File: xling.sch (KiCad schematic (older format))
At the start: 61 parts, among them J1 ISP, J2 USB_OTG, J3 Battery, Q1 NTR0202PL, SW1 BTN, SW2 BTN, SW3 BTN, U1 REX012864L, U2 ATmega1284P-AU, U3 MCP73831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

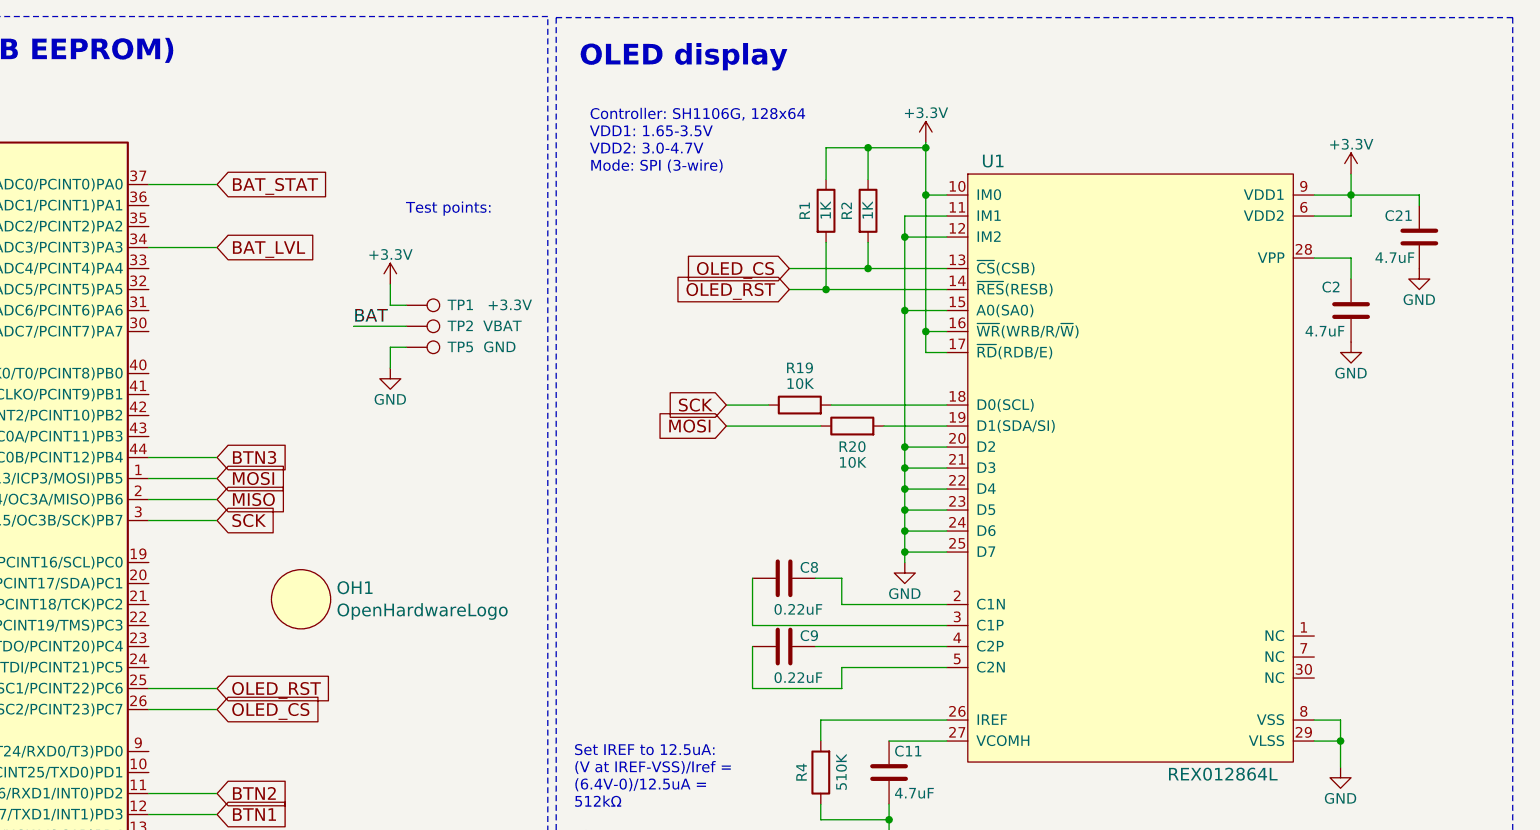
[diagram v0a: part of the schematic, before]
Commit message: patch 3.1: More checkpoints and 4-wire SPI.
This is the first commit after version adjustment and in a new
current/3.0 branch. All of the changes in the third iteration of the
Xling PCB will find their place in this branch.

Starting from Xling PCB v3.1, new checkpoints are available:

    +3.3V - output voltage of the power supply block and AP3401
            particularly;
    VBAT - Li-Ion battery voltage;
    SCK - SCK pin of the SPI;
    MOSI - MOSI pin of the SPI;
    CS - Chip-select pin of the OLED display;
    DC - Data/Command pin of the OLED display;
    RST - Reset pin of the OLED display;
    GND - Ground of the PCB.

And the display is connected via 4-wire SPI from now on.

Signed-off-by: Dmitry Salychev <dsl@mcusim.org>
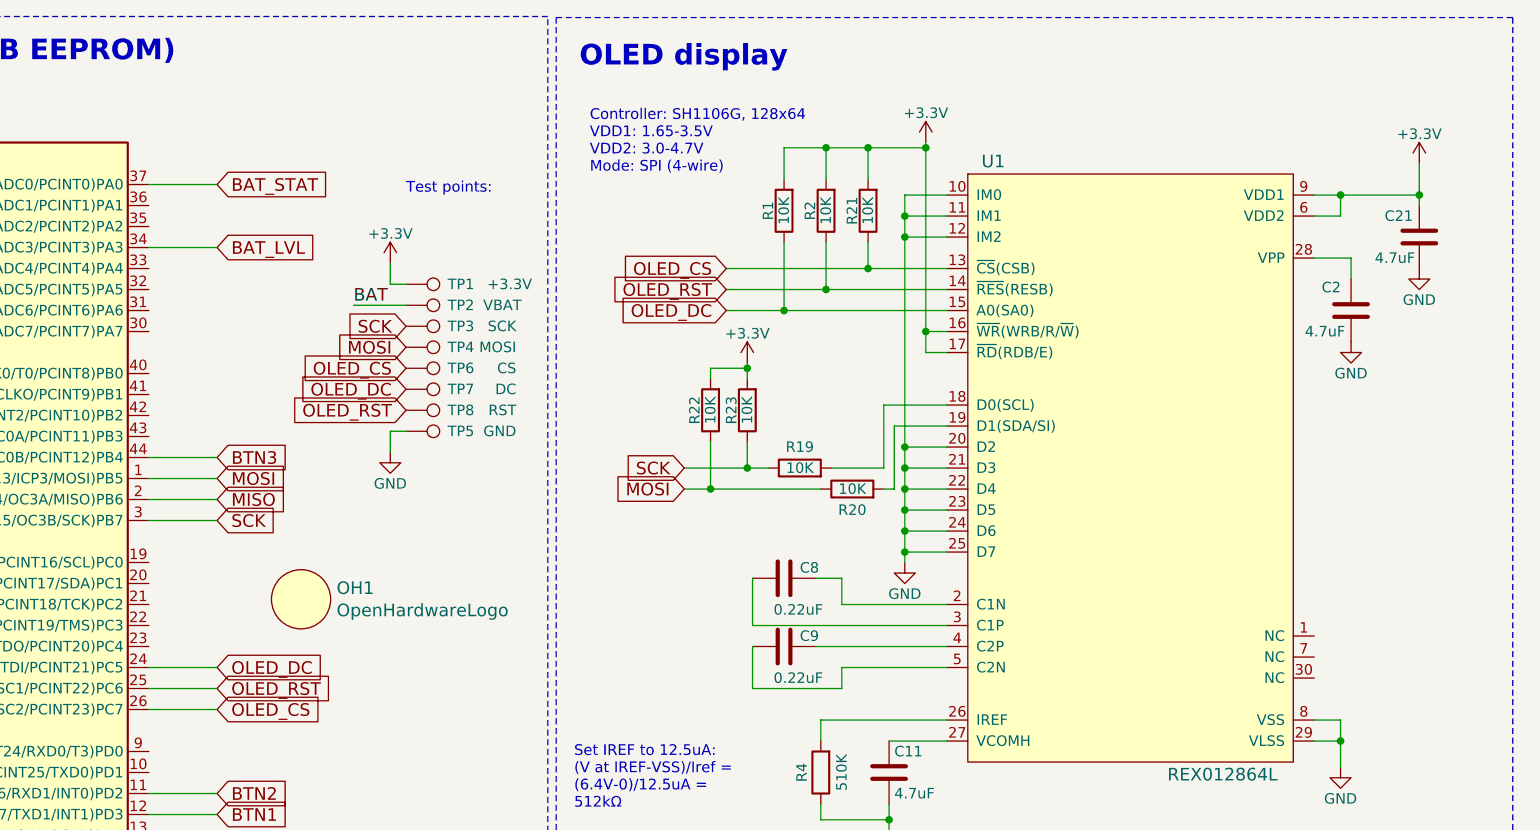
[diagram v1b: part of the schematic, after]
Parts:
- added R21, R22, R23: 10K, Xling Footprints:R_0603_1608Metric, symbol xling:R
- added TP3: SCK, Xling Footprints:TestPoint_Pad_D2.0mm, symbol Connector:TestPoint
- added TP4: MOSI, Xling Footprints:TestPoint_Pad_D2.0mm, symbol Connector:TestPoint
- added TP6: CS, Xling Footprints:TestPoint_Pad_D2.0mm, symbol Connector:TestPoint
- added TP7: DC, Xling Footprints:TestPoint_Pad_D2.0mm, symbol Connector:TestPoint
- added TP8: RST, Xling Footprints:TestPoint_Pad_D2.0mm, symbol Connector:TestPoint
- R1, R2: value 1K -> 10K; Model CRCW06031K00JNTABC -> 0603SAJ0103T5E
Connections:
- net +3V3: now also R1.2, R2.2, R21.2, R22.2, R23.2; no longer R1.1, R2.1, U1.10 (IM0)
- net GND: now also U1.10 (IM0); no longer U1.15 (A0(SA0))
- net MOSI: now also R22.1, TP4.1
- net OLED_CS: now also R21.1, TP6.1; no longer R2.2
- net OLED_RST: now also R2.1, TP8.1; no longer R1.2
- net SCK: now also R23.1, TP3.1
- net OLED_DC: now reaches U2.24 ((TDI/PCINT21)PC5)
- net OLED_DC: now also R1.1, U1.15 (A0(SA0)), TP7.1
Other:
- note added: "Controller: SH1106G, 128x64\nVDD1: 1.65-3.5V\nVDD2: 3.0-4.7V\nMode: SPI (4-wire)"
- note removed: "Controller: SH1106G, 128x64\nVDD1: 1.65-3.5V\nVDD2: 3.0-4.7V\nMode: SPI (3-wire)"
- moved on the sheet: R19, R20, TP1, TP2, TP5

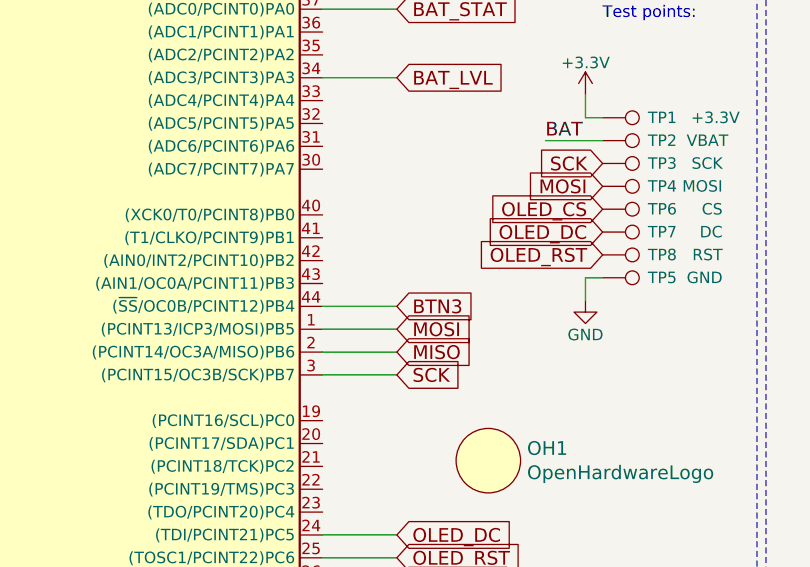
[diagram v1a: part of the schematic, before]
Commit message: patch 3.2: Minor PCB changes.
- Buttons are placed according to the new case configuration;
- BTN3 pin assigned to pin 42 (INT2) of the MCU;
- A new silkscreen artwork based on U2Pi's work from deviantart;
- A narrow deeping on the left is a bit wider;

Signed-off-by: Dmitry Salychev <dsl@mcusim.org>
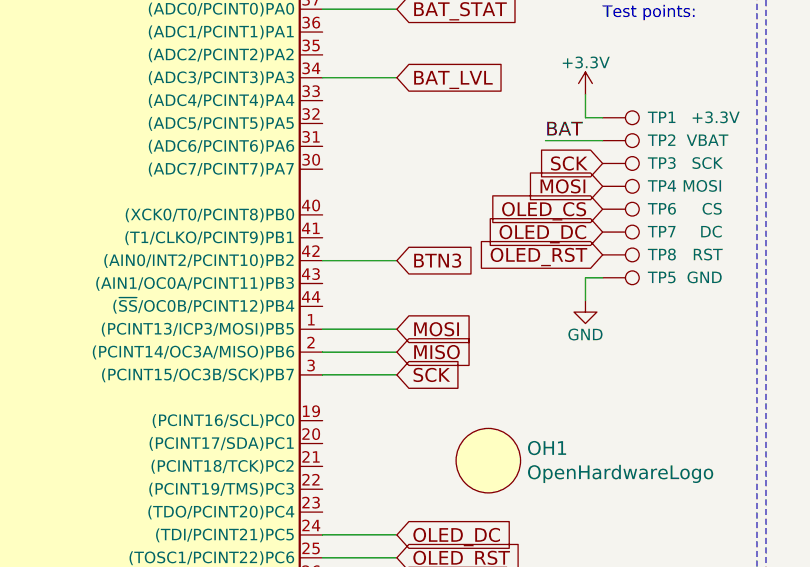
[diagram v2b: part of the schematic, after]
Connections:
- net BTN3: now also U2.42 ((AIN0/INT2/PCINT10)PB2); no longer U2.44 ((~SS~/OC0B/PCINT12)PB4)
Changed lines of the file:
@@
 Sheet 1 1
 Title "Xling, a tamagotchi-like toy"
-Date "2019-10-20"
-Rev "3.1"
+Date "2020-01-13"
+Rev "3.2"
 Comp ""
 Comment1 ""
 Comment2 ""
-Comment3 "Dmitry Salychev"
+Comment3 "Dmitry Salychev <dsl@mcusim.org>"
 Comment4 "Designed by"
 $EndDescr
@@
 Text GLabel 4525 4200 2    60   Input ~ 0
 BTN2
-Text GLabel 4525 2600 2    60   Input ~ 0
+Text GLabel 4525 2400 2    60   Input ~ 0
 BTN3
 Text GLabel 7925 5625 2    60   Input ~ 0
@@
 Wire Wire Line
 	4525 4200 4200 4200
-Wire Wire Line
-	4200 2600 4525 2600
 $Comp
 L xling:R R3
@@
 Wire Wire Line
 	7050 2650 7150 2650
+Wire Wire Line
+	4525 2400 4200 2400
 $EndSCHEMATC
